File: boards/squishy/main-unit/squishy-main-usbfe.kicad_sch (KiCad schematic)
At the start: 44 parts, among them J1 USB_C_Receptacle, U1 LFE5UM5G-45F-8BG381C, U10 FUSB302BMPX, U13 HD3SS460, U14 TPD4E02B04DQA, U15 TPD4E02B04DQA, U17 USB3318, U4 SP3400-02UTG, X2 13MHz, X3 200MHz

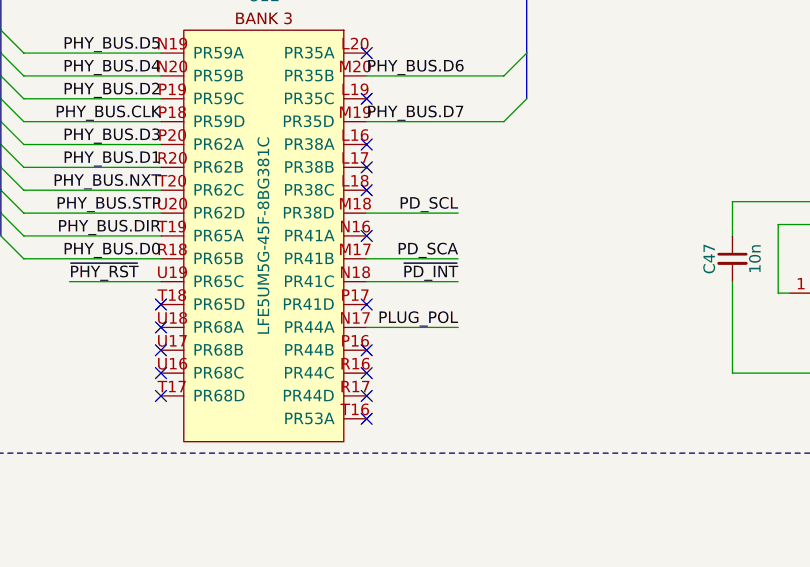
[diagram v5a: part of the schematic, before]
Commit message: squishy: main: A whole bunch of cleanup, also routed a large chunk of the supervisor
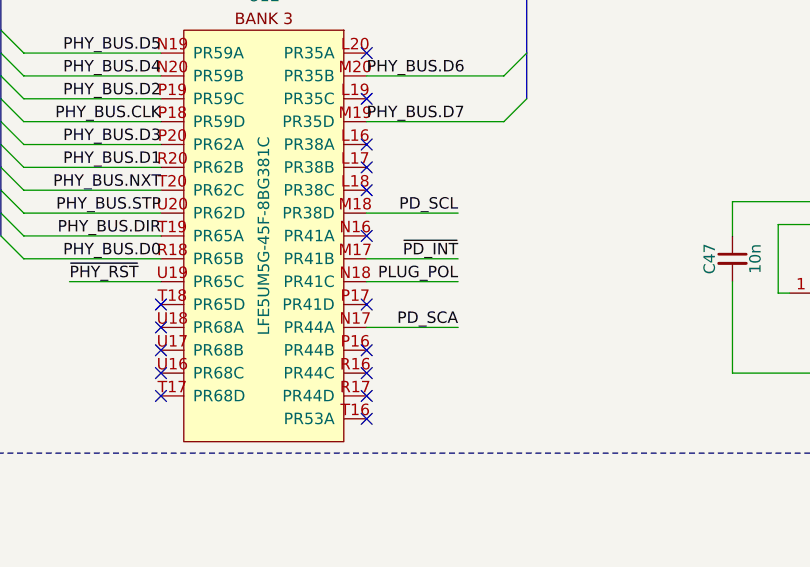
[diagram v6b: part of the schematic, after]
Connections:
- net PD_SCA: now also U1.N17 (PR44A); no longer U1.M17 (PR41B)
- net PLUG_POL: now also U1.N18 (PR41C); no longer U1.N17 (PR44A)
- net ~{PD_INT}: now also U1.M17 (PR41B); no longer U1.N18 (PR41C)
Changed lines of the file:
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@@
 	(wire
 		(pts
-			(xy 213.36 106.68) (xy 203.2 106.68)
+			(xy 213.36 101.6) (xy 203.2 101.6)
 		)
 		(stroke
@@
 	(wire
 		(pts
-			(xy 203.2 99.06) (xy 213.36 99.06)
+			(xy 203.2 106.68) (xy 213.36 106.68)
 		)
 		(stroke
@@
 	(wire
 		(pts
-			(xy 203.2 101.6) (xy 213.36 101.6)
+			(xy 203.2 99.06) (xy 213.36 99.06)
 		)
 		(stroke
@@
 	)
 	(label "PLUG_POL"
-		(at 213.36 106.68 180)
+		(at 213.36 101.6 180)
 		(fields_autoplaced yes)
 		(effects
@@
 	)
 	(label "~{PD_INT}"
-		(at 213.36 101.6 180)
+		(at 213.36 99.06 180)
 		(fields_autoplaced yes)
 		(effects
@@
 	)
 	(label "PD_SCA"
-		(at 213.36 99.06 180)
+		(at 213.36 106.68 180)
 		(fields_autoplaced yes)
 		(effects

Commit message: squishy: main: cleaning up the schematics, also routed the `SEPIC_GOOD` to the POR rather than just relying on the 5V from the SEPIC output to kick on the rest of the power tree
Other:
- note removed: "Cable Inserted"
- note removed: "Check Orientation"
- note removed: "Cont Sys Init"
- note removed: "FAIL/TIMEOUT"
- note removed: "INIT ULPI"
- note removed: "Indicate No Cable"
- note removed: "Indicate No Host"
- note removed: "Indicate USB2"
- note removed: "Indicate USB3"
- note removed: "NO"
- note removed: "PLUG_PRS=1"
- note removed: "SUCCESS"
- note removed: "Setup Mux"
- note removed: "Shutdown Transciver"
- note removed: "Shutdown ULPI"
- note removed: "Try USB2"
- note removed: "Try USB3"
- note removed: "USB Front-End Flow"
- note removed: "YES"
- moved on the sheet: C16, C17, C49, C91, C92, C93, R22, R44, R45, TP33, TP34, TP35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

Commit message: squishy: main: added proper tolerances to the resistors and capacitors
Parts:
- C16, C47, C57, C93: Tolerance (none) -> ±10% 25V
- C17, C49, C51, C52, C81, C83, C85, C91: Tolerance (none) -> ±10% 50V
- C3, C49, C50, C6, C92: Tolerance (none) -> ±20% 50V
- C48: Tolerance (none) -> ±10% 10V
- C82, C84: Tolerance (none) -> ±10% 16V
- F2: Tolerance (none) -> 63VDC
- R1, R11, R2, R22, R44, R45: Tolerance (none) -> ±1% 1/10W
- R5: Tolerance (none) -> ±1% 1/16W
